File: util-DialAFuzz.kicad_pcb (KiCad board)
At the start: 2 copper layers, 9.5 x 21.2 mm, 6 parts, among them J1 Conn_01x03_Pin, Q1 BC847, Q2 BC847

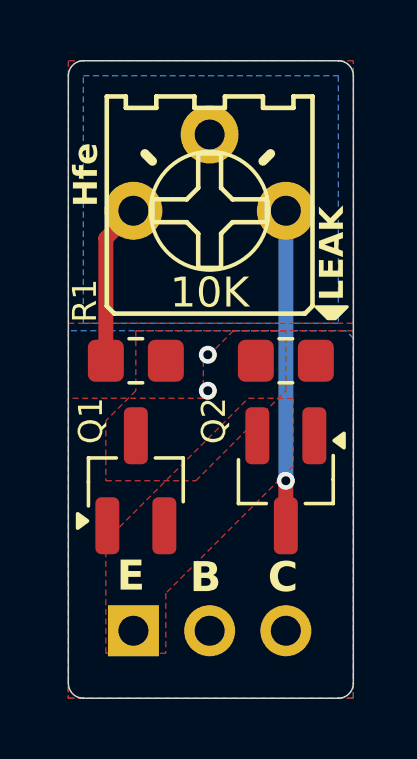
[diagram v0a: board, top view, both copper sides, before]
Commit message: Rework as Widlar hFE dial: Q1 diode-connected with 1M emitter trimmer, Q2 pass transistor
The first draft paralleled Q2 with a rheostat in its collector, which does
nothing until Q2 saturates and then collapses the effective hFE. Now Q1 is
diode-connected (C tied to B) with RV1 as a rheostat in its emitter, so it
steals base drive from Q2 in a Widlar split; effective hFE is roughly linear
in RV1 and scales with the host stage's bias current (1M reaches ~125 in a
50 uA collector-feedback stage). R1 dropped: the floor is not a stopper.
R2 2.2M collector-base (DNP) remains the leakage stand-in.

Co-Authored-By: Claude Fable 5.1 <noreply@anthropic.com>
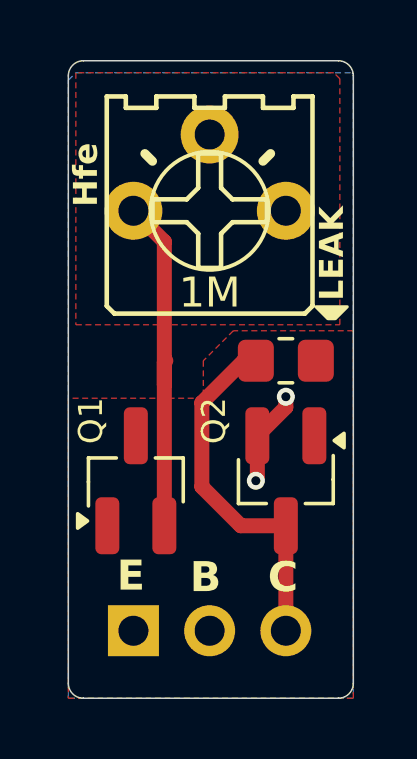
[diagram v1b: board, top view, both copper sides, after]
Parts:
- removed R1: 2.2K, Resistor_SMD:R_0805_2012Metric_Pad1.20x1.40mm_HandSolder
- RV1: value 10K -> 1M
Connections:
- Q1 pad 2: EMITTER -> Net-(Q1-E)
- Q1 pad 3: COLLECTOR -> BASE
- Q2 pad 3: Net-(Q2-C) -> COLLECTOR
- RV1 pad 1: Net-(R1-Pad2) -> Net-(Q1-E)
- RV1 pad 2: Net-(Q2-C) -> EMITTER
- RV1 pad 3: Net-(Q2-C) -> EMITTER
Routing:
- net COLLECTOR: track 0.00 -> 12.0 mm, vias 2 -> 0
- net Net-(Q1-E): track 0.00 -> 11.7 mm
- net Net-(Q2-C): track 10.5 -> 0.00 mm, vias 1 -> 0
- net Net-(R1-Pad2): track 5.38 -> 0.00 mm
- net EMITTER: track 0.00 -> 3.21 mm, vias 0 -> 2
- added copper zone on B.Cu, net EMITTER
- added copper zone on F.Cu, net Net-(Q1-E)
- removed copper zone on B.Cu, net COLLECTOR
- removed copper zone on F.Cu, net COLLECTOR
- removed copper zone on F.Cu, net EMITTER
- removed copper zone on B.Cu, net Net-(Q2-C)
- removed copper zone on F.Cu, net Net-(R1-Pad2)

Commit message: Remove dangling track stub on the Q1 emitter net
Co-Authored-By: Claude Fable 5.1 <noreply@anthropic.com>
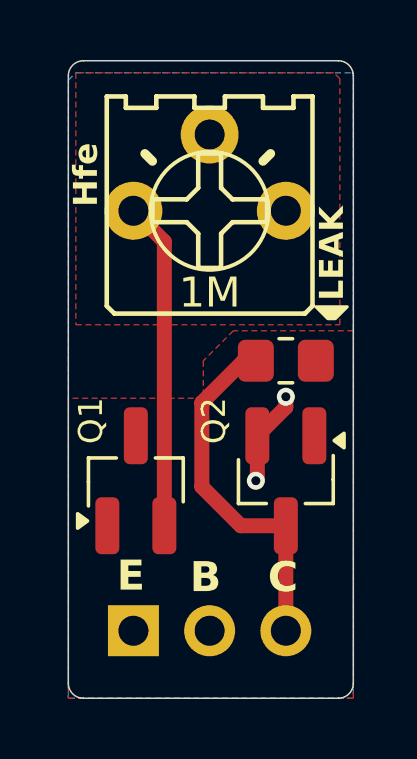
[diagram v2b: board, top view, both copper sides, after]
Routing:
- net Net-(Q1-E): track 11.7 -> 10.9 mm
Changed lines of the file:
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@@
-	)
-	(segment
-		(start 98.95 79.05)
-		(end 99 79)
-		(width 0.5)
-		(layer "F.Cu")
-		(net "Net-(Q1-E)")
 	)
 	(segment
@@
 	)
 	(segment
-		(start 98.95 79.8)
+		(start 98.95 84.5)
 		(end 98.95 75.03)
 		(width 0.5)
 		(layer "F.Cu")
-		(net "Net-(Q1-E)")
-	)
-	(segment
-		(start 98.95 79.8)
-		(end 98.95 79.05)
-		(width 0.5)
-		(layer "F.Cu")
-		(net "Net-(Q1-E)")
-	)
-	(segment
-		(start 98.95 84.5)
-		(end 98.95 79.8)
-		(width 0.5)
-		(layer "F.Cu")
